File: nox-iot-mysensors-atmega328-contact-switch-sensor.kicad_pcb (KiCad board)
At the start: 2 copper layers, 22 x 75 mm, 13 parts, among them U1 ATmega328-PU, U3 NRF24L01, Y1 16Mhz

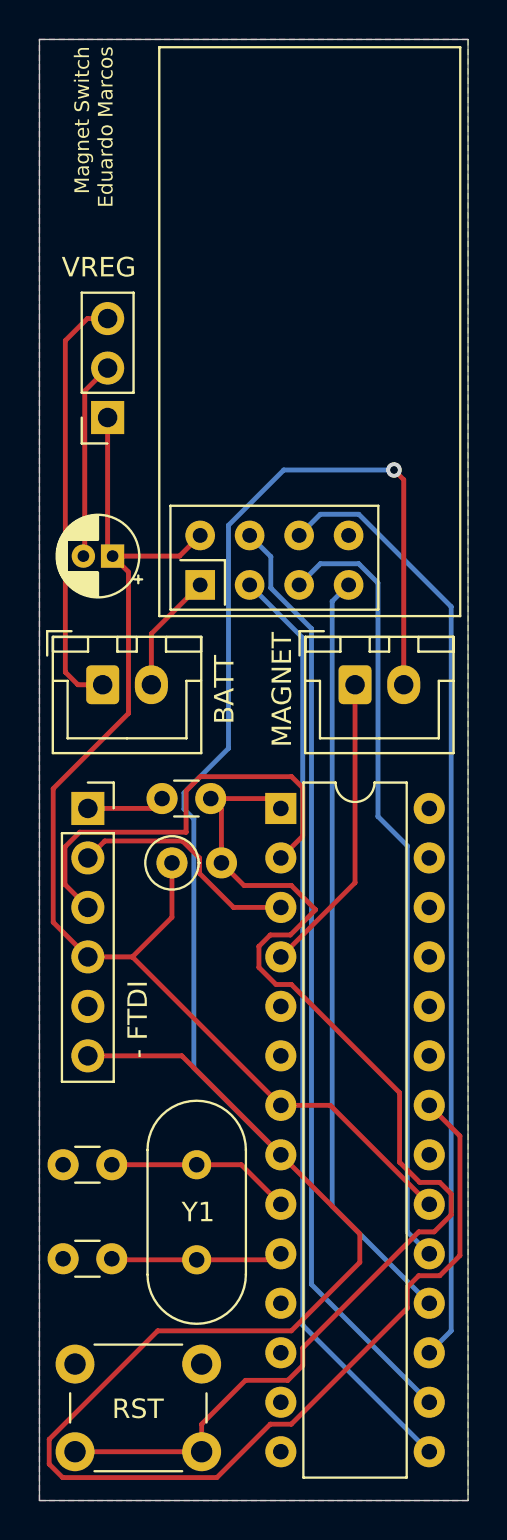
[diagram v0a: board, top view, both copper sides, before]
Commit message: voltage divider for battery sensor
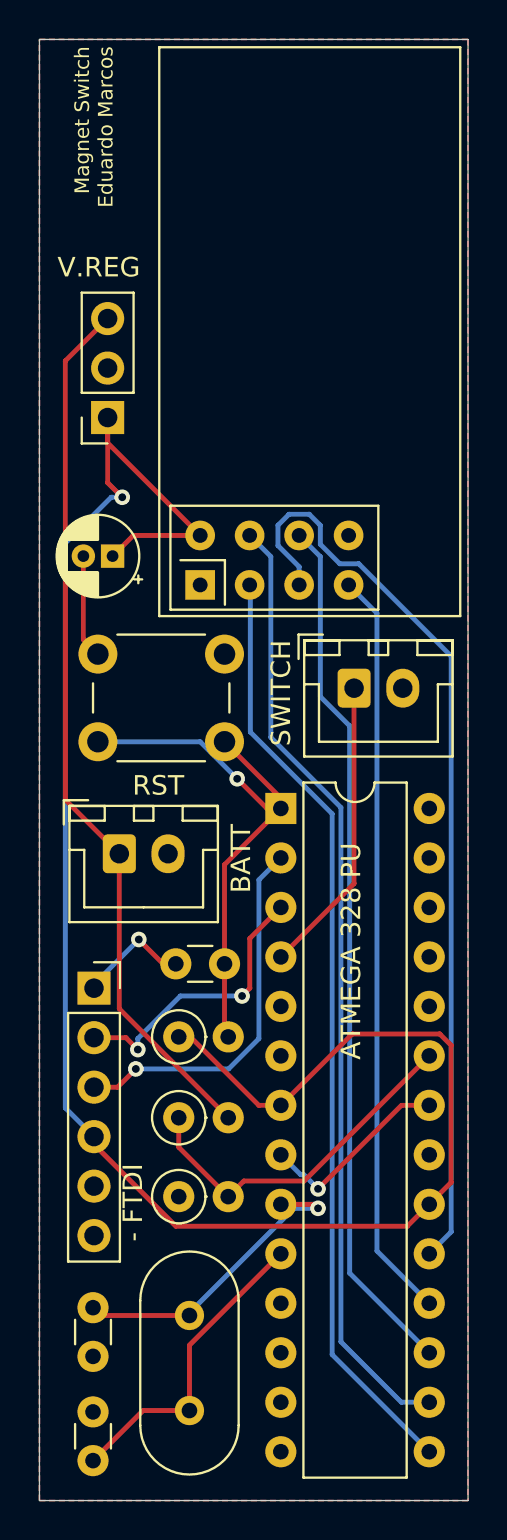
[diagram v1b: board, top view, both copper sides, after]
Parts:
- removed U1: ATmega328-PU, Package_DIP:DIP-28_W7.62mm
- added ATMEGA 328 PU: ATmega328-PU, Package_DIP:DIP-28_W7.62mm, F.Cu at (72.4, 109.5)
- added R2: 1M, Resistor_THT:R_Axial_DIN0207_L6.3mm_D2.5mm_P2.54mm_Vertical, F.Cu at (67.2, 125.3)
- added R3: 430K, Resistor_THT:R_Axial_DIN0207_L6.3mm_D2.5mm_P2.54mm_Vertical, F.Cu at (67.2, 129.4)
- moved RST 36.5 mm to (69.5, 106.0)
- moved C1 9.96 mm to (62.8, 137.6), turned to 90 degrees
- moved - FTDI 9.23 mm to (62.8, 118.7)
- moved R1 8.94 mm to (67.2, 121.2)
- moved BATT 8.72 mm to (64.1, 111.8)
- moved C4 8.51 mm to (67.0, 117.5)
- moved C2 8.01 mm to (62.8, 140.4), turned to 270 degrees
- moved Y1 7.75 mm to (67.7, 135.5)
- moved SWITCH 0.18 mm to (76.2, 103.3)
- renumbered MAGNET to SWITCH, VREG to V.REG
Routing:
- net GND: track 147.8 -> 15.5 mm
- net /RST: track 62.5 -> 28.4 mm, vias 0 -> 1
- net +3V3: track 63.9 -> 98.0 mm, vias 0 -> 1
- net +BATT: track 21.8 -> 45.4 mm
- net /BATT_SENSOR: track 0.00 -> 18.4 mm
- net /SCK: track 40.4 -> 47.4 mm
- net Net-(C2-Pad2): track 9.26 -> 16.0 mm
- net Net-(C1-Pad2): track 9.52 -> 16.1 mm, vias 0 -> 1
- net /MOSI: track 49.0 -> 44.7 mm
- net /TX: track 22.8 -> 19.2 mm, vias 0 -> 1
- net /RX: track 12.1 -> 14.7 mm, vias 0 -> 2
- net Net-(C4-Pad1): track 4.02 -> 5.87 mm, vias 0 -> 1
- net /CNS: track 48.3 -> 49.2 mm
- net /MISO: track 39.3 -> 38.6 mm

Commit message: updated with voltage divider value
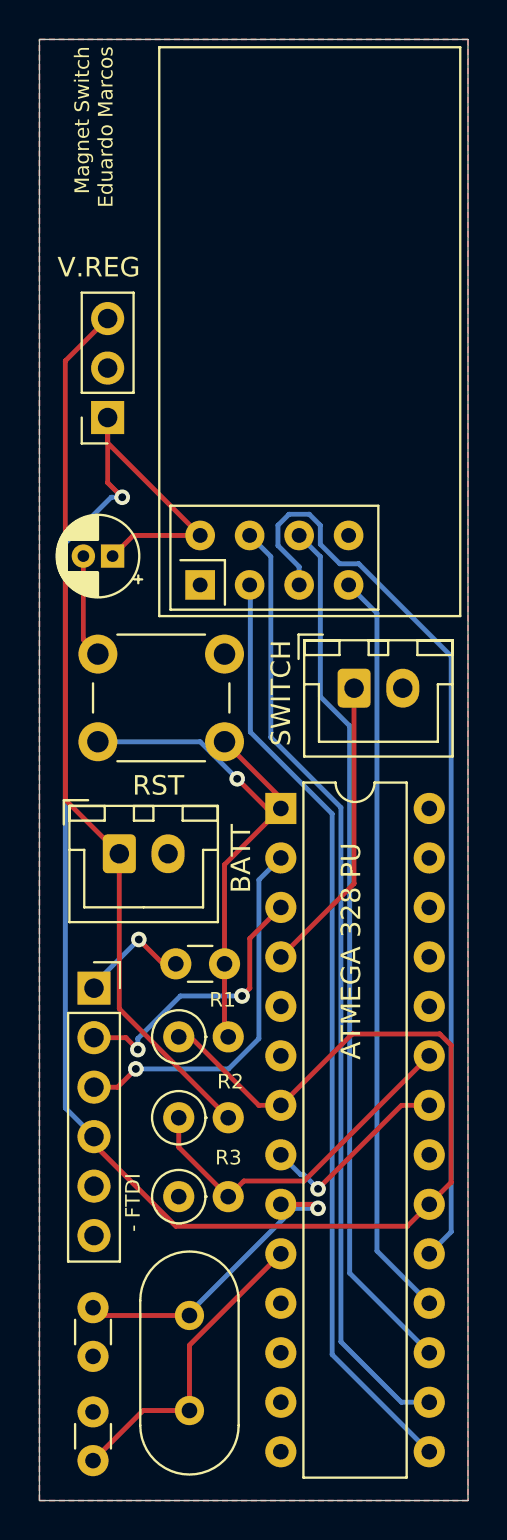
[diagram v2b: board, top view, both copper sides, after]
